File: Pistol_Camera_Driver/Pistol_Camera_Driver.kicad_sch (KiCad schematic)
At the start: 50 parts, among them J1 Screw_Terminal_01x02, J2 Conn_01x08, J3 Screw_Terminal_01x02, J4 Screw_Terminal_01x02, J5 Conn_01x04_Female, J6 Joystick, J7 Screw_Terminal_01x02, J8 Screw_Terminal_01x03, M1 Fan, Q1 IRLML6402, U1 LM7805_TO220, U2 LM317_TO-263, U3 Raspberri_Pi_Pico, U4 DRV8834PWP, U5 DRV8834PWP, U6 LDD-700L, U7 LDD-700L

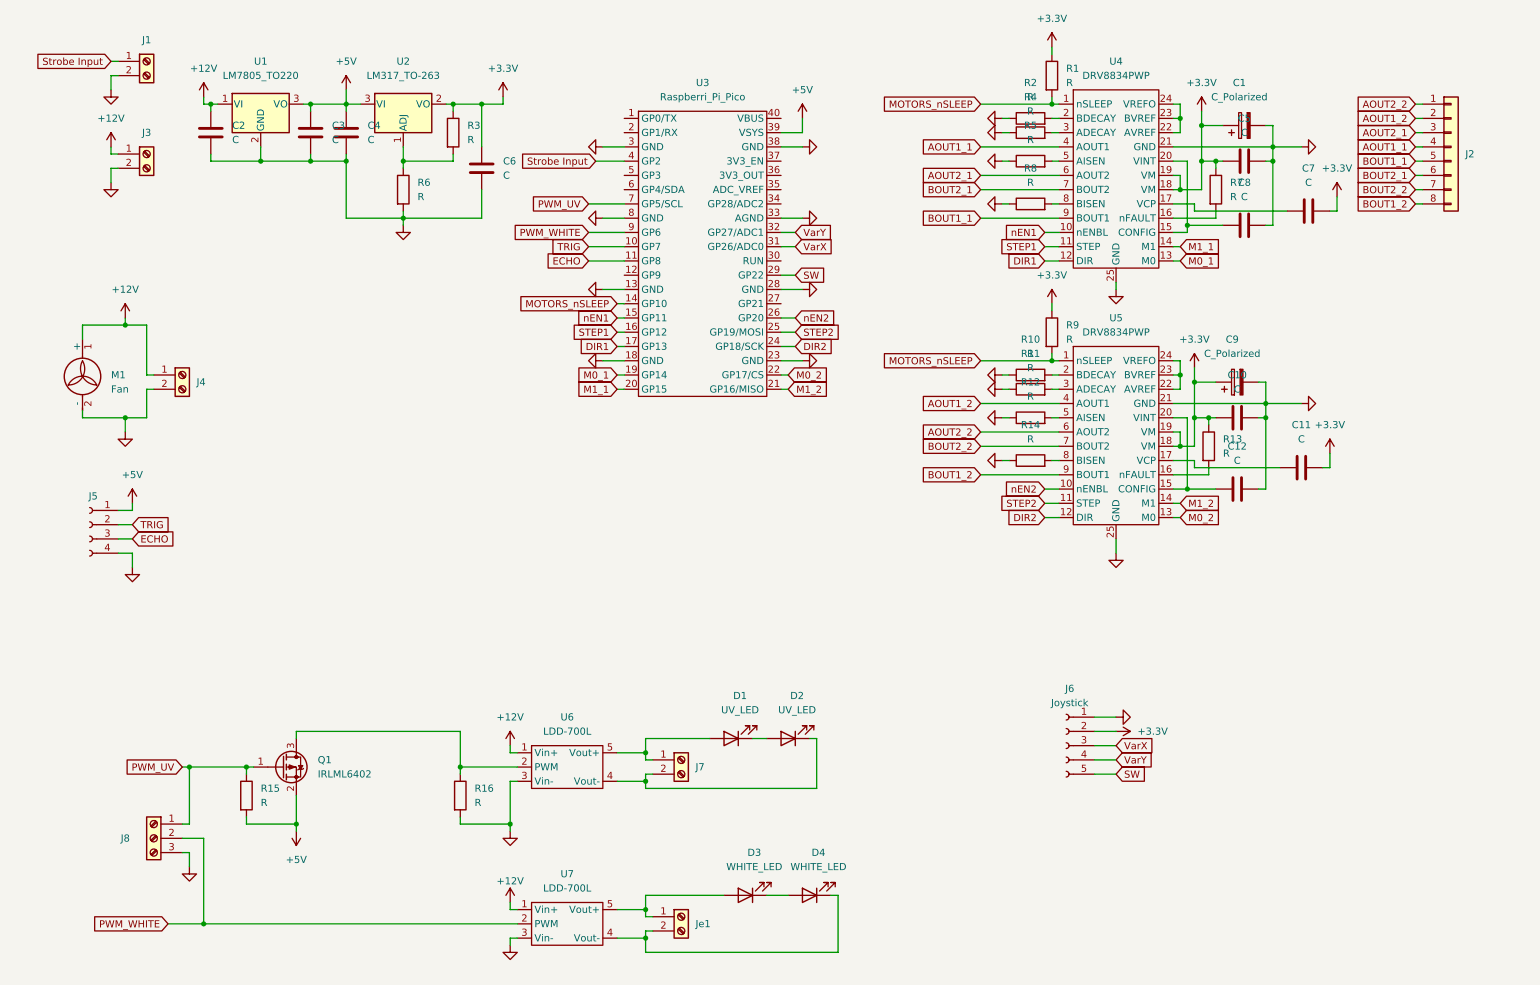
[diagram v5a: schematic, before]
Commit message: v0.7 vircuit has been corrected
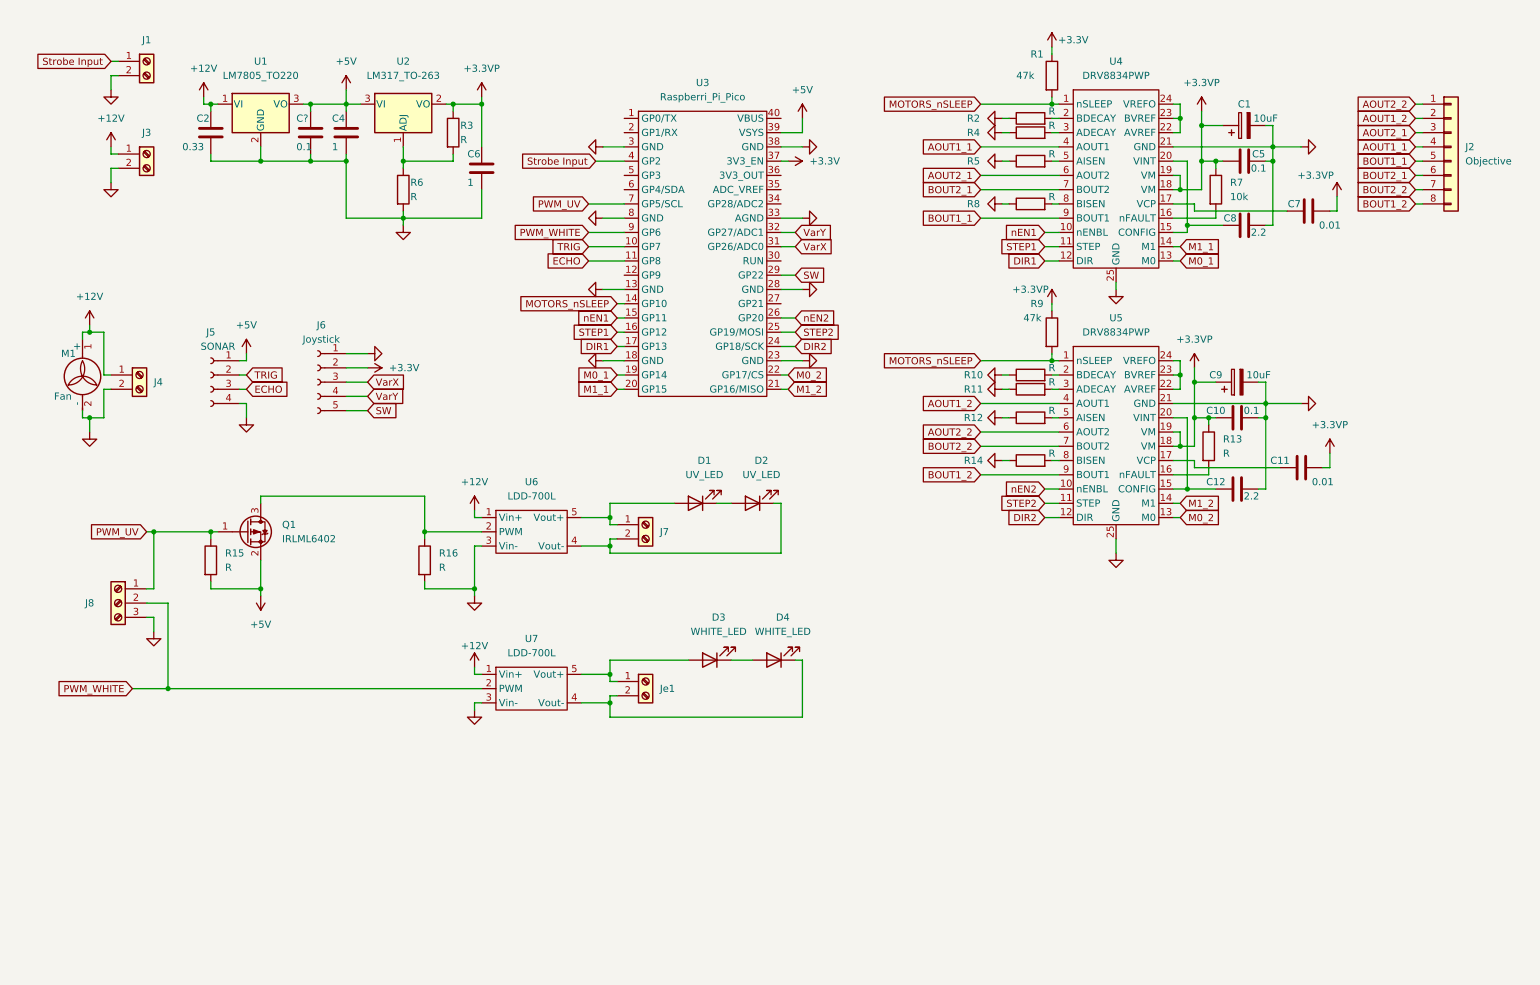
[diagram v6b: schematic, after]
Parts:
- C1, C9: value C_Polarized -> 10uF
- C10, C5: value C -> 0.1
- C11, C7: value C -> 0.01
- C12, C8: value C -> 2.2
- C2: value C -> 0.33
- C4, C6: value C -> 1
- C?: renamed from C3; value C -> 0.1
- J2: value Conn_01x08 -> Objective
- J5: value Conn_01x04_Female -> SONAR
- R1, R9: value R -> 47k
- R7: value R -> 10k
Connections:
- net +3V3: now also U3.37 (3V3_EN); no longer C1.1, C10.1, C11.2, C5.2, C6.1, C7.2, C9.1, R13.1, R3.1, R7.1, R9.1, U2.2 (VO), U4.18 (VM), U4.19 (VM), U5.18 (VM), U5.19 (VM)
- new net +3.3VP: C1.1, C10.1, C11.2, C5.2, C6.1, C7.2, C9.1, R13.1, R3.1, R7.1, R9.1, U2.2 (VO), U4.18 (VM), U4.19 (VM), U5.18 (VM), U5.19 (VM)
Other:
- moved on the sheet: D1, D2, D3, D4, J4, J5, J6, J7, J8, Je1, Q1, R15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

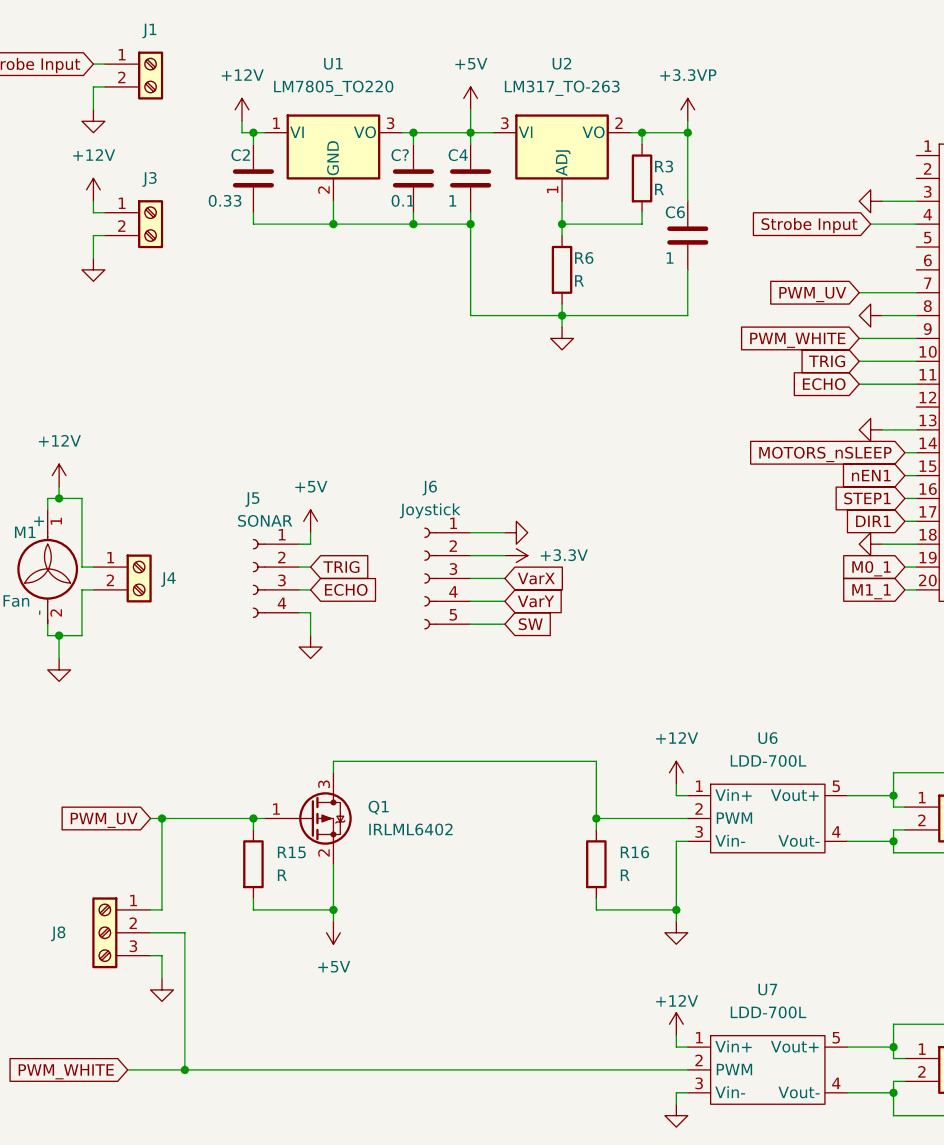
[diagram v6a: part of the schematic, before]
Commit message: v0.72 level translaors have been added
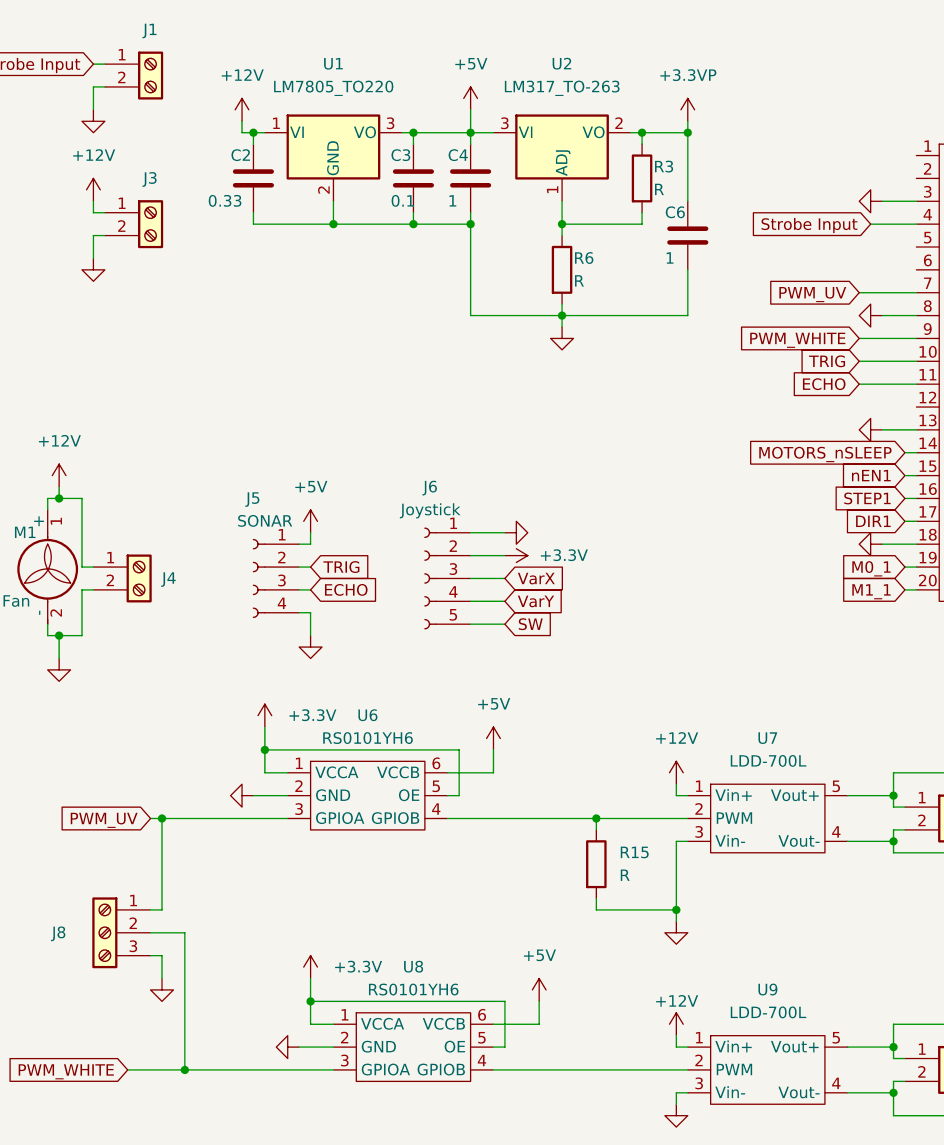
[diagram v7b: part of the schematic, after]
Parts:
- removed Q1: IRLML6402, Package_TO_SOT_SMD:SOT-23, symbol Transistor_FET:IRLML6402
- removed R15: R, Resistor_SMD:R_0603_1608Metric_Pad0.98x0.95mm_HandSolder, symbol Device:R
- added U6, U8: RS0101YH6, Package_TO_SOT_SMD:SOT-23-6_Handsoldering, symbol Shield_Emergent:RS0101YH6
- gave numbers to parts that had none: 1
- renumbered R16 to R15, U6 to U7, U7 to U9
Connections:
- net +3V3: now also U6.1 (VCCA), U6.5 (OE), U8.1 (VCCA), U8.5 (OE)
- net +5V: now also U6.6 (VCCB), U8.6 (VCCB)
- net GND: now also U6.2 (GND), U8.2 (GND)
- net PWM_UV: now also U6.3 (GPIOA)
- net PWM_WHITE: now also U8.3 (GPIOA); no longer U9.2 (PWM)
- net at R15.1, U7.2 (PWM): now also U6.4 (GPIOB)
- new net: U8.4 (GPIOB), U9.2 (PWM)

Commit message: v0.8 first decomposition is completed
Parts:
- removed J8: Screw_Terminal_01x03, Connector_PinSocket_2.54mm:PinSocket_1x03_P2.54mm_Vertical, symbol Connector:Screw_Terminal_01x03
- added D5, D6: UV_LED, symbol Device:LED
- added J8: Screw_Terminal_01x04, Connector_PinHeader_2.54mm:PinHeader_1x04_P2.54mm_Vertical, symbol Connector:Screw_Terminal_01x04
- added J9: Screw_Terminal_01x02, Connector_PinSocket_2.54mm:PinSocket_1x02_P2.54mm_Vertical, symbol Connector:Screw_Terminal_01x02
- added R16: R, Resistor_SMD:R_0603_1608Metric_Pad0.98x0.95mm_HandSolder, symbol Device:R
- added U10: RS0101YH6, Package_TO_SOT_SMD:SOT-23-6_Handsoldering, symbol Shield_Emergent:RS0101YH6
- added U11: LDD-700L, Shield_Emergent:LDD-700L, symbol Shield_Emergent:LDD-700L
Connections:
- net +12V: now also U11.1 (Vin+)
- net +3V3: now also U10.1 (VCCA), U10.5 (OE)
- net +5V: now also U10.6 (VCCB)
- net GND: now also J8.4 (Pin_4), R16.2, U10.2 (GND), U11.3 (Vin-)
- net PWM_UV: now also J8.1 (Pin_1)
- net PWM_WHITE: now also J8.2 (Pin_2)
- net VarX: now also J6.4 (Pin_4); no longer J6.3 (Pin_3)
- net VarY: now also J6.3 (Pin_3); no longer J6.4 (Pin_4)
- net PWM_RED: now reaches U3.6 (GP4/SDA)
- net PWM_RED: now also J8.3 (Pin_3), U10.3 (GPIOA)
- new net: D5.1 (K), D6.2 (A)
- new net: D5.2 (A), J9.1 (Pin_1), U11.5 (Vout+)
- new net: D6.1 (K), J9.2 (Pin_2), U11.4 (Vout-)
- new net: R16.1, U10.4 (GPIOB), U11.2 (PWM)
